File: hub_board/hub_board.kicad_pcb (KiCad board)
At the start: 4 copper layers, 75 x 75 mm, 11 parts, among them J1 Fingers, J2 Fingers, J3 Fingers, J4 Fingers, J5 1473149-4, U1 AP2112K-3.3TRG1

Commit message: Finish hub board layout
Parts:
- added R1: 1K, Resistor_SMD:R_0603_1608Metric, B.Cu at (58.1, 69.1)
- added R2: 1K, Resistor_SMD:R_0603_1608Metric, B.Cu at (58.1, 66.3)
- added REF**: MountingHole_3.2mm_M3, MountingHole:MountingHole_3.2mm_M3, F.Cu at (70.0, 54.0)
- added REF**: MountingHole_3.2mm_M3, MountingHole:MountingHole_3.2mm_M3, F.Cu at (37.5, 5.00)
- added REF**: MountingHole_3.2mm_M3, MountingHole:MountingHole_3.2mm_M3, F.Cu at (5.00, 54.0)
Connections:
- J5 pad 109: unconnected-(J5-Pad109) -> /LED2
- J5 pad 111: unconnected-(J5-Pad111) -> /LED1
- J5 pad 85: /LED1 -> unconnected-(J5-Pad85)
- J5 pad 87: /LED2 -> unconnected-(J5-Pad87)
- J5 pad SH1: unconnected-(J5B-SHIELD-PadSH1) -> GND
- J5 pad SH2: unconnected-(J5B-SHIELD__1-PadSH2) -> GND
- RJ1 pad 15: unconnected-(RJ1-Pad15) -> GND
- RJ1 pad 16: unconnected-(RJ1-Pad16) -> GND
- USB1 pad 7: (no net) -> GND
- USB1 pad 8: (no net) -> GND
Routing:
- net /CLK: track 47.1 -> 229.5 mm
- net +5V: track 16.2 -> 76.1 mm, vias 0 -> 2
- net /M35: track 0.00 -> 49.5 mm, vias 0 -> 1
- net /M34: track 0.00 -> 48.5 mm, vias 0 -> 1
- net /M33: track 0.00 -> 46.9 mm, vias 0 -> 1
- net /M23: track 0.00 -> 46.6 mm, vias 0 -> 1
- net /M22: track 0.00 -> 46.4 mm, vias 0 -> 1
- net /M21: track 0.00 -> 45.7 mm, vias 0 -> 1
- net /M32: track 0.00 -> 44.6 mm, vias 0 -> 1
- net /M18: track 0.00 -> 44.5 mm
- net /M17: track 0.00 -> 44.5 mm
- net /M16: track 0.00 -> 44.4 mm
- net /M30: track 0.00 -> 44.3 mm
- net /M15: track 0.00 -> 44.3 mm
- net /M14: track 0.00 -> 44.2 mm
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- added copper zone on In2.Cu, net +3V3
- added copper zone on B.Cu, net +5V

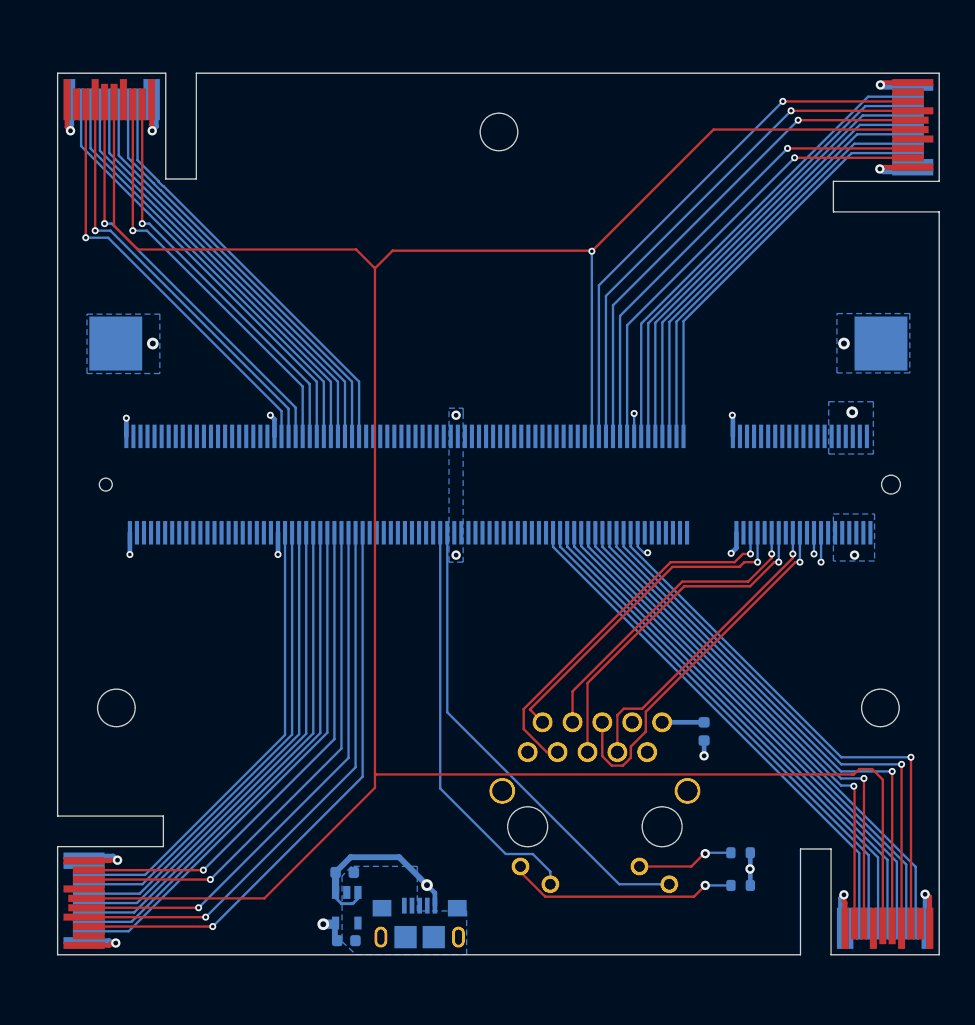
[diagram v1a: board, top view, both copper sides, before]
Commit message: Fix DDR2 connector position & reroute; add test points
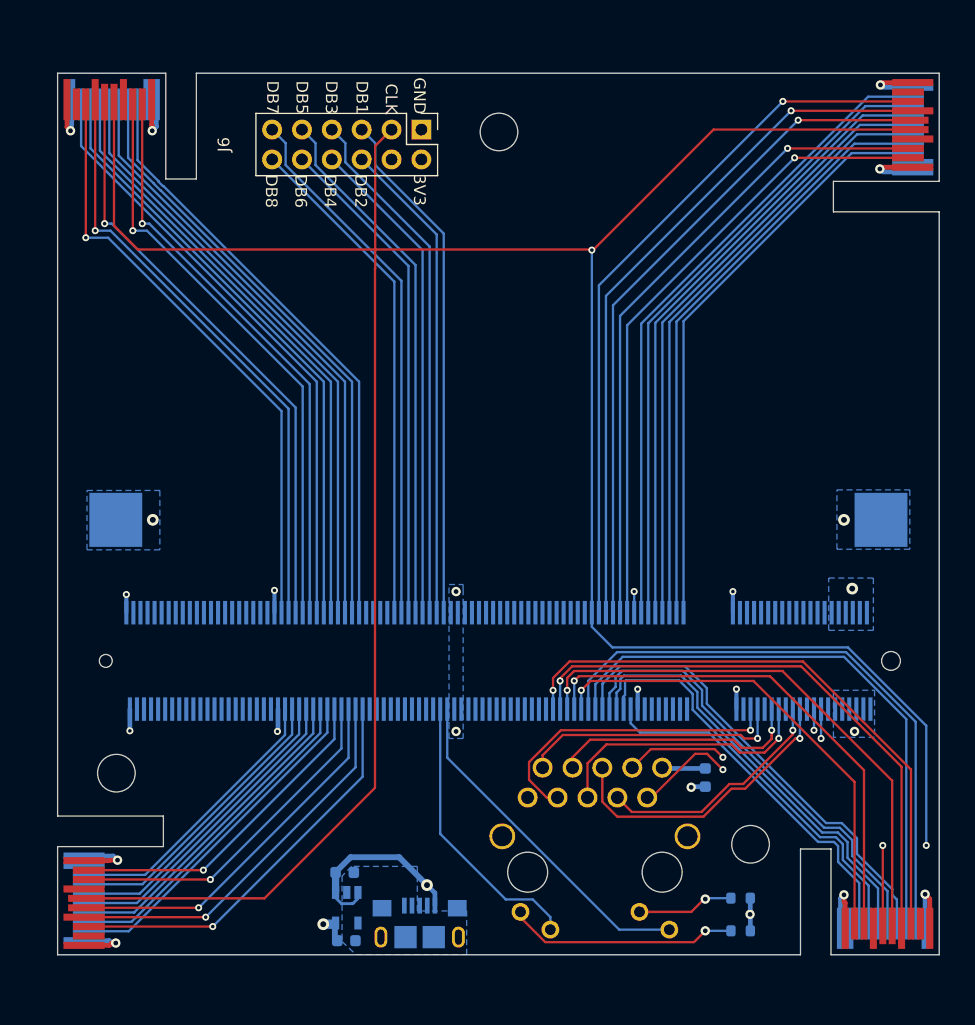
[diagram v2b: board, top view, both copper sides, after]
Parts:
- added J6: Test Points, Connector_PinHeader_2.54mm:PinHeader_2x06_P2.54mm_Vertical, F.Cu at (30.9, 4.80)
- moved REF** 16.0 mm to (59.0, 65.6)
- moved J5 15.0 mm to (37.5, 50.0)
- moved REF** 5.55 mm to (5.00, 59.5)
- moved C4 3.93 mm to (55.1, 59.9)
- moved R1 3.86 mm to (58.1, 73.0)
- moved R2 3.86 mm to (58.1, 70.2)
- moved RJ1 3.86 mm to (45.7, 66.0)
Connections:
- J5 pad 110: unconnected-(J5-Pad110) -> /DBG1
- J5 pad 112: unconnected-(J5-Pad112) -> /DBG2
- J5 pad 114: unconnected-(J5-Pad114) -> /DBG3
- J5 pad 116: unconnected-(J5-Pad116) -> /DBG4
- J5 pad 118: unconnected-(J5-Pad118) -> /DBG5
- J5 pad 120: unconnected-(J5-Pad120) -> /DBG6
- J5 pad 122: unconnected-(J5-Pad122) -> /DBG7
- J5 pad 124: unconnected-(J5-Pad124) -> /DBG8
- J5 pad 57: /M23 -> /M12
- J5 pad 59: /M22 -> /M13
- J5 pad 61: /M21 -> /M14
- J5 pad 63: /M20 -> /M15
- J5 pad 65: /M19 -> /M16
- J5 pad 67: /M18 -> /M17
- J5 pad 69: /M17 -> /M18
- J5 pad 71: /M16 -> /M19
- J5 pad 73: /M15 -> /M20
- J5 pad 75: /M14 -> /M21
- J5 pad 77: /M13 -> /M22
- J5 pad 79: /M12 -> /M23
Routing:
- net /DBG7: track 0.00 -> 45.7 mm
- net /DBG5: track 0.00 -> 45.1 mm
- net /DBG3: track 0.00 -> 44.5 mm
- net /DBG1: track 0.00 -> 44.0 mm
- net /DBG8: track 0.00 -> 42.9 mm
- net /DBG6: track 0.00 -> 42.3 mm
- net /DBG4: track 0.00 -> 41.8 mm
- net /DBG2: track 0.00 -> 41.2 mm
- net /CLK: track 229.5 -> 253.2 mm, vias 1 -> 3
- net /M45: track 35.5 -> 50.5 mm
- net /M38: track 36.2 -> 51.2 mm
- net /M24: track 38.8 -> 23.8 mm
- net /M30: track 44.3 -> 29.3 mm
- net /M28: track 42.5 -> 27.5 mm
- net /M9: track 43.0 -> 58.0 mm
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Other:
- board text added: "3V3"
- board text added: "CLK"
- board text added: "DB1"
- board text added: "DB2"
- board text added: "DB3"
- board text added: "DB4"
- board text added: "DB5"
- board text added: "DB6"
- board text added: "DB7"
- board text added: "DB8"
- board text added: "GND"

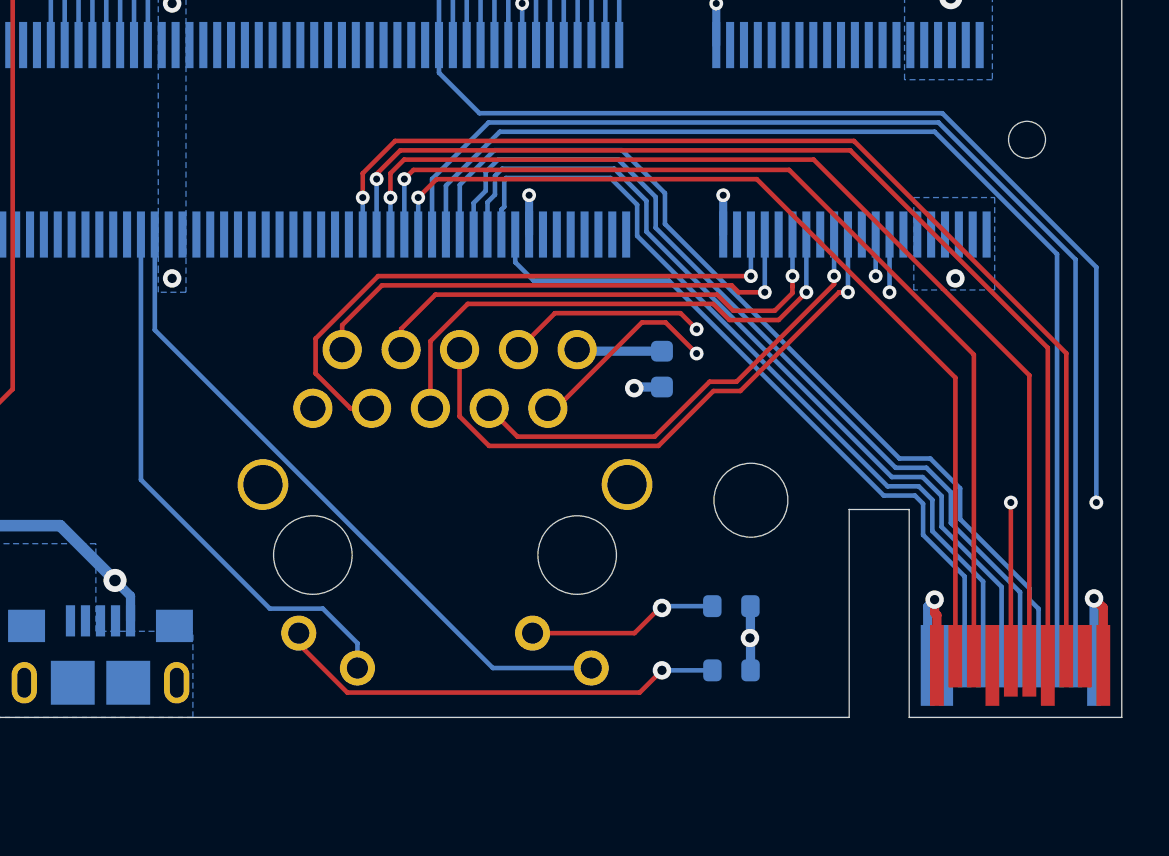
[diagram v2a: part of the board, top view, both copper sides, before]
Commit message: Flip Ethernet port to front side
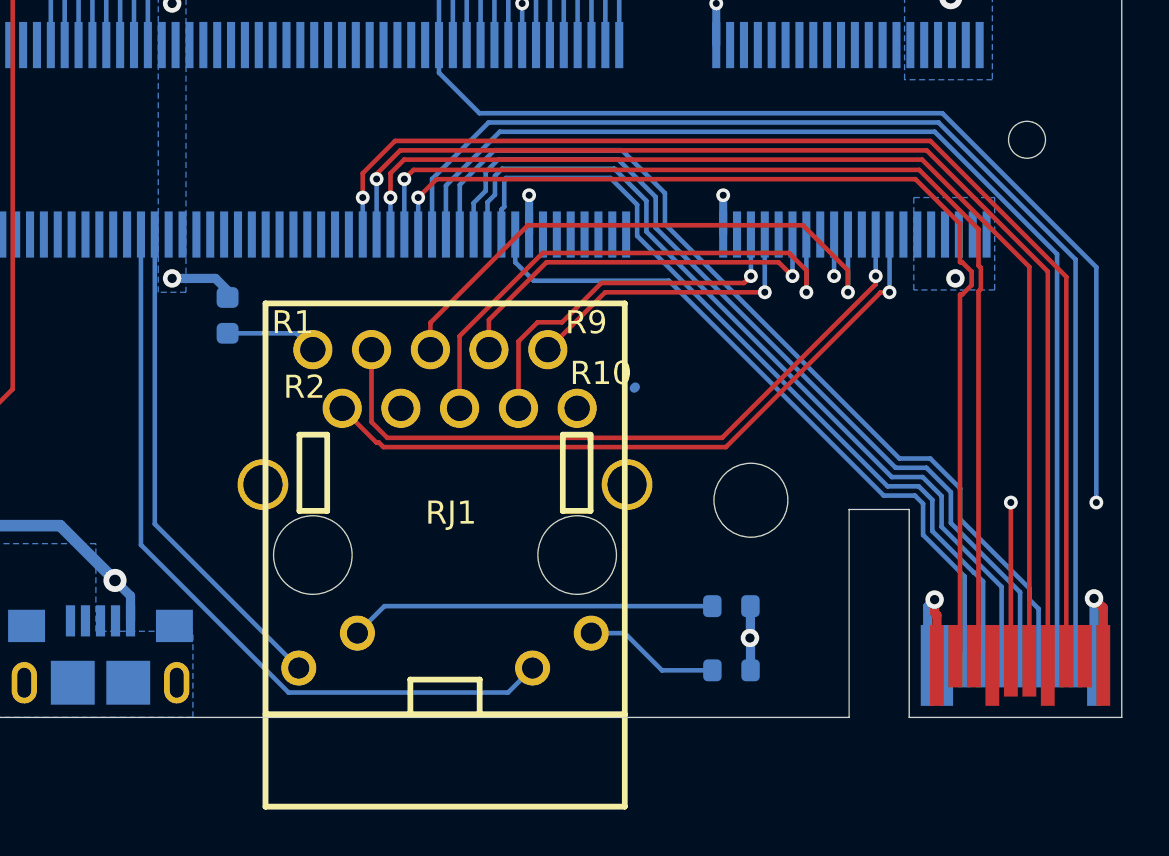
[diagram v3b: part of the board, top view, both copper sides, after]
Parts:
- RJ1: moved to F.Cu
- moved C4 18.9 mm to (36.3, 57.6), turned to 90 degrees
- turned RJ1 to 0 degrees
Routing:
- net Net-(RJ1-LED1+): track 19.6 -> 5.91 mm, vias 1 -> 0
- net /ETH1_4P: track 26.3 -> 15.9 mm
- net /ETH1_1N: track 20.1 -> 30.1 mm, vias 2 -> 1
- net /ETH1_4N: track 22.7 -> 12.9 mm
- net /LED1: track 24.0 -> 33.5 mm
- net /ETH1_1P: track 20.5 -> 29.7 mm, vias 2 -> 1
- net /LED2: track 29.1 -> 21.3 mm
- net Net-(RJ1-LED2+): track 8.26 -> 15.8 mm, vias 1 -> 0
- net /ETH1_2P: track 20.3 -> 25.1 mm
- net /M19: track 40.8 -> 45.5 mm
- net /ETH1_3N: track 21.6 -> 17.5 mm
- net /M20: track 43.6 -> 47.2 mm
- net /M21: track 46.8 -> 49.5 mm
- net /M23: track 50.5 -> 52.5 mm
- net /M22: track 49.4 -> 51.3 mm
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
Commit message: Redo layout (wip)
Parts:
- removed R1, R2: 1K, Resistor_SMD:R_0603_1608Metric
- removed USB1: 10118193-0001LF, Hub:MICRO-USB-SMD_10118193-0001LF
- added C3: 10u, Capacitor_SMD:C_0603_1608Metric, B.Cu at (-2.40, 47.6)
- added J7: 54-00166, Hub:TENSILITY_54-00166, F.Cu at (47.5, 4.65)
- C1, C2, C4, J5, U1: moved to F.Cu
- RJ1: moved to B.Cu
- moved C1 78.3 mm to (59.0, 3.50), turned to -90 degrees
- moved U1 73.4 mm to (56.5, 4.85)
- moved C2 69.1 mm to (58.3, 7.75)
- moved J6 68.5 mm to (55.0, 69.0)
- moved RJ1 58.9 mm to (31.4, 8.79)
- moved REF** 56.1 mm to (16.9, 4.70)
- moved C4 46.4 mm to (21.9, 13.4)
- moved REF** 34.9 mm to (70.2, 17.3)
- moved REF** 24.4 mm to (35.0, 70.5)
- moved J5 7.00 mm to (37.5, 57.0), turned to 180 degrees
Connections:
- J5 pad 109: /LED2 -> /DBG8
- J5 pad 110: /DBG1 -> /LED2
- J5 pad 111: /LED1 -> /DBG7
- J5 pad 112: /DBG2 -> /LED1
- J5 pad 113: unconnected-(J5-Pad113) -> /DBG6
- J5 pad 114: /DBG3 -> unconnected-(J5-Pad114)
- J5 pad 115: unconnected-(J5-Pad115) -> /DBG5
- J5 pad 116: /DBG4 -> unconnected-(J5-Pad116)
- J5 pad 117: unconnected-(J5-Pad117) -> /DBG4
- J5 pad 118: /DBG5 -> unconnected-(J5-Pad118)
- J5 pad 119: unconnected-(J5-Pad119) -> /DBG3
- J5 pad 120: /DBG6 -> unconnected-(J5-Pad120)
- J5 pad 121: unconnected-(J5-Pad121) -> /DBG2
- J5 pad 122: /DBG7 -> unconnected-(J5-Pad122)
- J5 pad 123: unconnected-(J5-Pad123) -> /DBG1
- J5 pad 124: /DBG8 -> unconnected-(J5-Pad124)
- J5 pad 133: /M35 -> /M12
- J5 pad 134: /M36 -> /M11
- J5 pad 135: /M34 -> /M13
- J5 pad 136: /M37 -> /M10
- J5 pad 137: /M33 -> /M14
- J5 pad 138: /M38 -> /M9
- J5 pad 139: /M32 -> /M15
- J5 pad 140: /M39 -> /M8
- J5 pad 141: /M31 -> /M16
- J5 pad 142: /M40 -> /M7
- J5 pad 143: /M30 -> /M17
- J5 pad 144: /M41 -> /M6
- J5 pad 145: /M29 -> /M18
- J5 pad 146: /M42 -> /M5
- J5 pad 147: /M28 -> /M19
- J5 pad 148: /M43 -> /M4
- J5 pad 149: /M27 -> /M20
- J5 pad 150: /M44 -> /M3
- J5 pad 151: /M26 -> /M21
- J5 pad 152: /M45 -> /M2
- J5 pad 153: /M25 -> /M22
- J5 pad 154: /M46 -> /M1
- J5 pad 155: /M24 -> /M23
- J5 pad 156: /M47 -> /M0
- J5 pad 22: /ETH2_2N -> /ETH2_2P
- J5 pad 24: /ETH2_2P -> /ETH2_2N
- J5 pad 34: /ETH2_4N -> /ETH2_4P
- J5 pad 36: /ETH2_4P -> /ETH2_4N
- J5 pad 42: /M0 -> /M47
- J5 pad 44: /M1 -> /M46
- J5 pad 46: /M2 -> /M45
- J5 pad 48: /M3 -> /M44
- J5 pad 50: /M4 -> /M43
- J5 pad 52: /M5 -> /M42
- J5 pad 54: /M6 -> /M41
- J5 pad 57: /M12 -> /M24
- J5 pad 58: /M7 -> /M40
- J5 pad 59: /M13 -> /M25
- J5 pad 60: /M8 -> /M39
- J5 pad 61: /M14 -> /M26
- J5 pad 62: /M9 -> /M38
- J5 pad 63: /M15 -> /M27
- J5 pad 64: /M10 -> /M37
- J5 pad 65: /M16 -> /M28
- J5 pad 66: /M11 -> /M36
- J5 pad 67: /M17 -> /M29
- J5 pad 69: /M18 -> /M30
- J5 pad 71: /M19 -> /M31
- J5 pad 73: /M20 -> /M32
- J5 pad 75: /M21 -> /M33
- J5 pad 77: /M22 -> /M34
- J5 pad 79: /M23 -> /M35
- RJ1 pad R2: /ETH1_1P -> /ETH2_1P
- RJ1 pad R3: /ETH1_1N -> /ETH2_1N
- RJ1 pad R4: /ETH1_2P -> /ETH2_2P
- RJ1 pad R5: /ETH1_2N -> /ETH2_2N
- RJ1 pad R6: /ETH1_3P -> /ETH2_3P
- RJ1 pad R7: /ETH1_3N -> /ETH2_3N
- RJ1 pad R8: /ETH1_4P -> /ETH2_4P
- RJ1 pad R9: /ETH1_4N -> /ETH2_4N
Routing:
- net /ETH2_4P: track 0.00 -> 47.6 mm
- net /ETH2_4N: track 0.00 -> 47.5 mm
- net /ETH2_3P: track 0.00 -> 47.3 mm
- net /ETH2_3N: track 0.00 -> 47.2 mm
- net /ETH2_2P: track 0.00 -> 47.0 mm
- net /ETH2_2N: track 0.00 -> 46.9 mm
- net /ETH2_1P: track 0.00 -> 46.6 mm
- net /ETH2_1N: track 0.00 -> 46.6 mm
- net /DBG7: track 45.7 -> 0.00 mm
- net /DBG5: track 45.1 -> 0.00 mm
- net /DBG3: track 44.5 -> 0.00 mm
- net /DBG1: track 44.0 -> 0.00 mm
- net /DBG8: track 42.9 -> 0.00 mm
- net /DBG6: track 42.3 -> 0.00 mm
- net /DBG4: track 41.8 -> 0.00 mm
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- added copper zone on F.Cu, net +5V
- added copper zone on F.Cu, net GND
- removed copper zone on B.Cu, net +5V
- removed copper zone on B.Cu, net GND

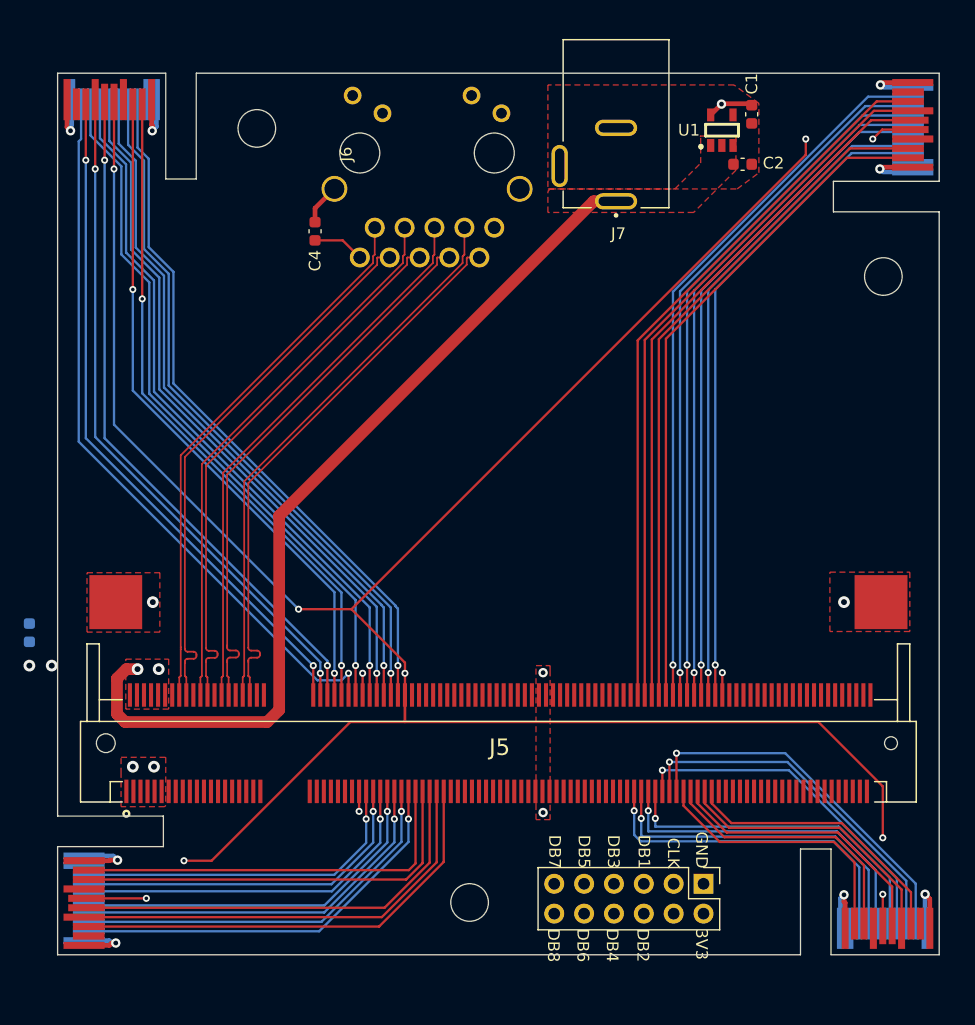
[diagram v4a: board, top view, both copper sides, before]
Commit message: Flip ethernet port & fix routing
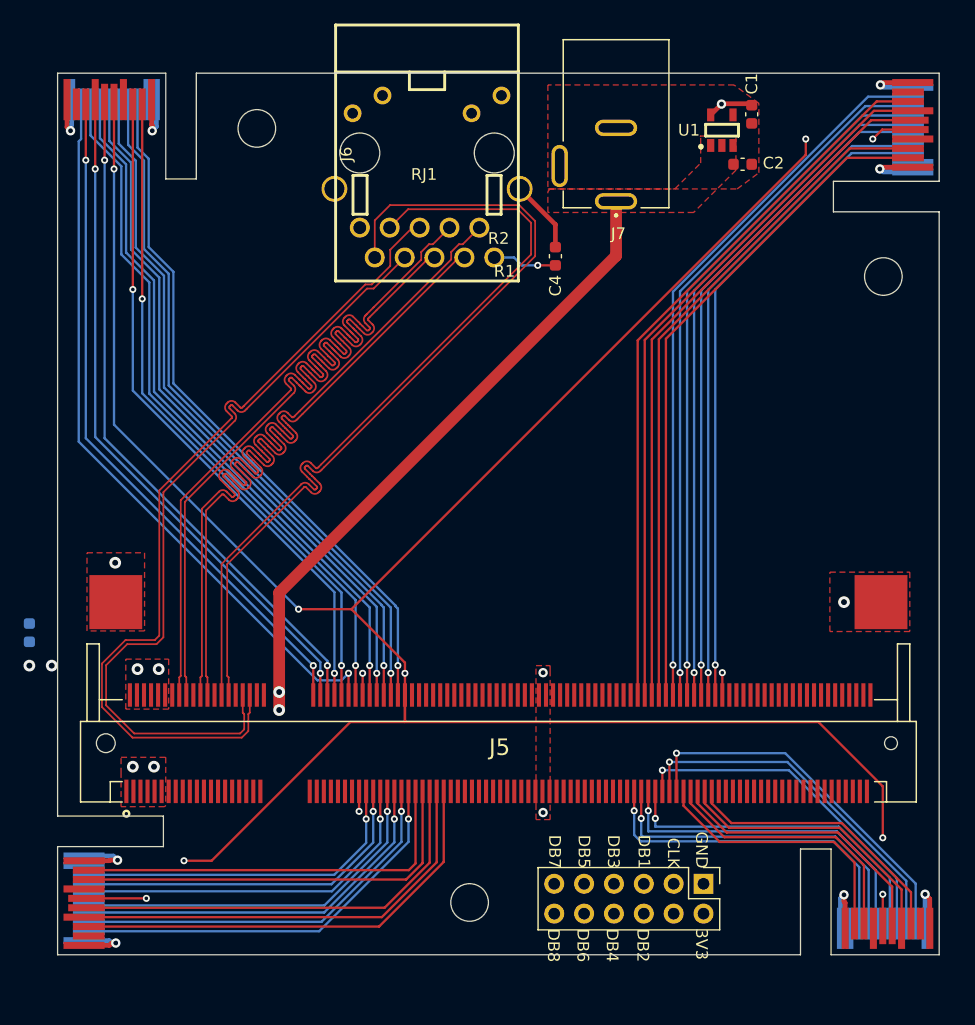
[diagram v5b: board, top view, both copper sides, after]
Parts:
- RJ1: moved to F.Cu
- moved C4 20.6 mm to (42.4, 15.6)
- turned RJ1 to 180 degrees
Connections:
- J5 pad 16: /ETH2_1P -> /ETH2_2P
- J5 pad 18: /ETH2_1N -> /ETH2_2N
- J5 pad 22: /ETH2_2P -> /ETH2_1P
- J5 pad 24: /ETH2_2N -> /ETH2_1N
- J5 pad 28: /ETH2_3P -> /ETH2_4P
- J5 pad 30: /ETH2_3N -> /ETH2_4N
- J5 pad 34: /ETH2_4P -> /ETH2_3N
- J5 pad 36: /ETH2_4N -> /ETH2_3P
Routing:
- net /ETH2_1P: track 46.6 -> 73.4 mm
- net /ETH2_3P: track 47.3 -> 72.8 mm
- net /ETH2_2P: track 47.0 -> 72.5 mm
- net /ETH2_4N: track 47.5 -> 73.0 mm
- net /ETH2_1N: track 46.6 -> 70.4 mm
- net /ETH2_2N: track 46.9 -> 69.5 mm
- net /ETH2_3N: track 47.2 -> 68.1 mm
- net +5V: track 76.2 -> 55.5 mm, vias 4 -> 6
- net /ETH2_4P: track 47.6 -> 68.1 mm
- net GND: track 33.0 -> 35.7 mm
- net Net-(RJ1-CT): track 4.41 -> 5.48 mm, vias 0 -> 1
- added copper zone on In2.Cu, net +5V
